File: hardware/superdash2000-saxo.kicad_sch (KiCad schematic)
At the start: 7 parts, among them J1 Molex 34691-0161, U1 L7805

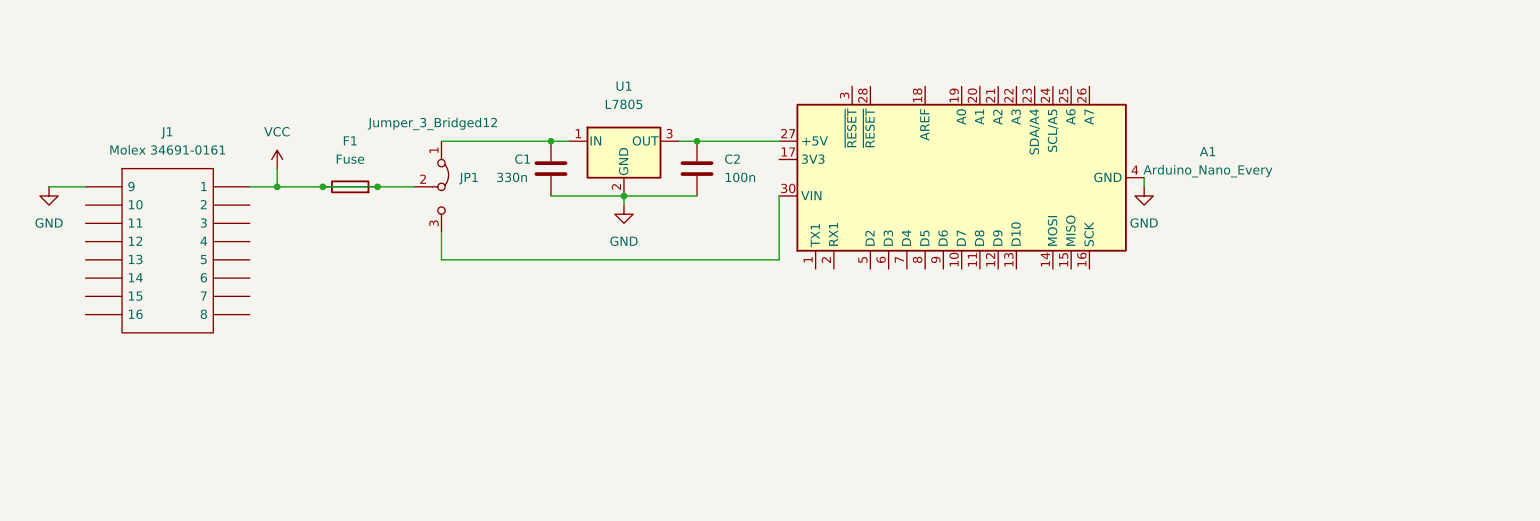
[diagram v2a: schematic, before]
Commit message: hardware: Update schematics
VCC -> +BATT
Add +5V label
Add LCD-SCL label
Add LCD-SDA label

Signed-off-by: Thomas Antonini <antonini.thomas@gmail.com>
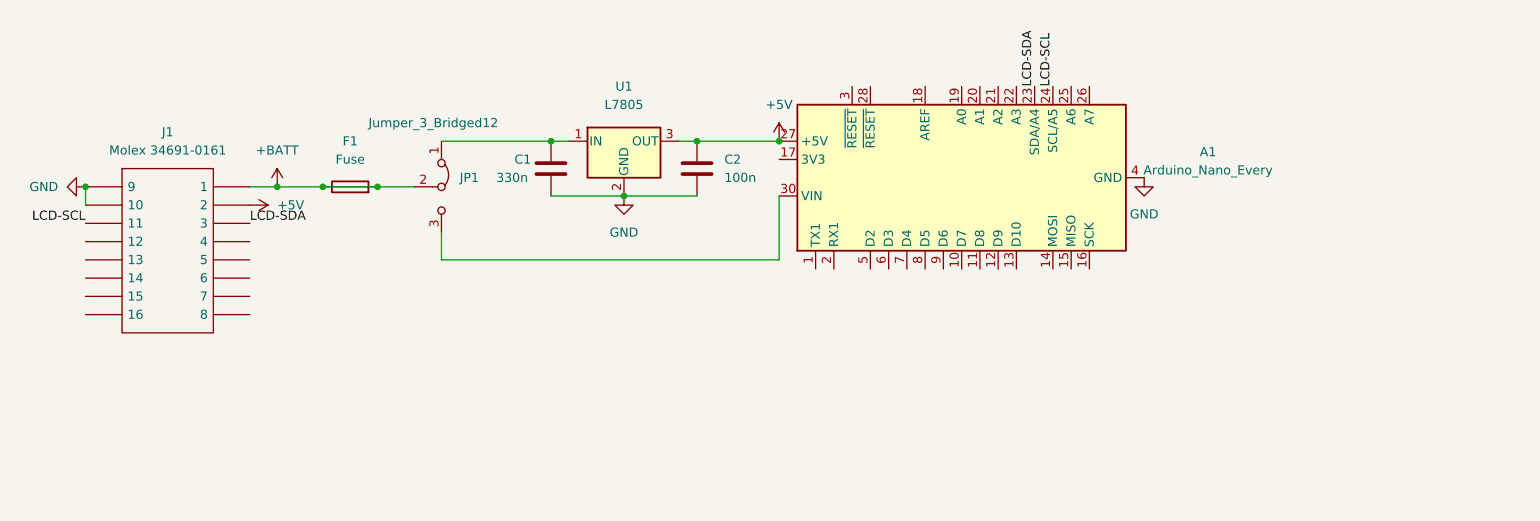
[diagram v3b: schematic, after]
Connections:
- net GND: now also J1.10
- net +5V: now reaches A1.27 (+5V), C2.1, U1.3 (OUT)
- net +5V: now also J1.2
- net LCD-SDA: now reaches A1.23 (SDA/A4)
- net LCD-SDA: now also J1.3
- net LCD-SCL: now reaches A1.24 (SCL/A5)
- net LCD-SCL: now also J1.11
- net VCC renamed +BATT
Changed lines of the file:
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@@
   (junction (at 64.77 64.77) (diameter 0) (color 0 0 0 0)
   )
+  (junction (at 134.62 58.42) (diameter 0) (color 0 0 0 0)
+  )
   (junction (at 123.19 58.42) (diameter 0) (color 0 0 0 0)
   )
   (junction (at 113.03 66.04) (diameter 0) (color 0 0 0 0)
   )
+  (junction (at 38.1 64.77) (diameter 0) (color 0 0 0 0)
+  )
   (junction (at 102.87 58.42) (diameter 0) (color 0 0 0 0)
   )
@@
     (stroke (width 0) (type default) (color 0 0 0 0))
   )
-  (wire (pts (xy 64.77 62.23) (xy 64.77 64.77))
-    (stroke (width 0) (type default) (color 0 0 0 0))
-  )
   (wire (pts (xy 78.74 64.77) (xy 83.82 64.77))
     (stroke (width 0) (type default) (color 0 0 0 0))
@@
     (stroke (width 0) (type default) (color 0 0 0 0))
   )
-  (wire (pts (xy 185.42 63.5) (xy 185.42 64.77))
-    (stroke (width 0) (type default) (color 0 0 0 0))
-  )
   (wire (pts (xy 71.12 64.77) (xy 78.74 64.77))
     (stroke (width 0) (type default) (color 0 0 0 0))
@@
     (stroke (width 0) (type default) (color 0 0 0 0))
   )
-  (wire (pts (xy 33.02 64.77) (xy 38.1 64.77))
-    (stroke (width 0) (type default) (color 0 0 0 0))
-  )
   (wire (pts (xy 102.87 66.04) (xy 113.03 66.04))
     (stroke (width 0) (type default) (color 0 0 0 0))
   )
-  (wire (pts (xy 113.03 66.04) (xy 113.03 67.31))
-    (stroke (width 0) (type default) (color 0 0 0 0))
-  )
   (wire (pts (xy 123.19 58.42) (xy 120.65 58.42))
     (stroke (width 0) (type default) (color 0 0 0 0))
@@
     (stroke (width 0) (type default) (color 0 0 0 0))
   )
+  (wire (pts (xy 38.1 64.77) (xy 38.1 67.31))
+    (stroke (width 0) (type default) (color 0 0 0 0))
+  )
   (wire (pts (xy 64.77 64.77) (xy 71.12 64.77))
     (stroke (width 0) (type default) (color 0 0 0 0))
@@
     (stroke (width 0) (type default) (color 0 0 0 0))
   )
-  (symbol (lib_id "power:GND") (at 185.42 64.77 0) (unit 1)
-    (in_bom yes) (on_board yes) (fields_autoplaced)
-    (property "Reference" "#PWR0101" (id 0) (at 185.42 71.12 0)
-      (effects (font (size 1.27 1.27)) hide)
-    )
-    (property "Value" "GND" (id 1) (at 185.42 69.85 0))
-    (property "Footprint" "" (id 2) (at 185.42 64.77 0)
-      (effects (font (size 1.27 1.27)) hide)
-    )
-    (property "Datasheet" "" (id 3) (at 185.42 64.77 0)
-      (effects (font (size 1.27 1.27)) hide)
-    )
-    (pin "1")
-  )
-  (symbol (lib_id "power:GND") (at 33.02 64.77 0) (unit 1)
-    (in_bom yes) (on_board yes) (fields_autoplaced)
-    (property "Reference" "#PWR?" (id 0) (at 33.02 71.12 0)
-      (effects (font (size 1.27 1.27)) hide)
-    )
-    (property "Value" "GND" (id 1) (at 33.02 69.85 0))
-    (property "Footprint" "" (id 2) (at 33.02 64.77 0)
-      (effects (font (size 1.27 1.27)) hide)
-    )
-    (property "Datasheet" "" (id 3) (at 33.02 64.77 0)
-      (effects (font (size 1.27 1.27)) hide)
-    )
-    (pin "1")
-  )
-  (symbol (lib_id "power:GND") (at 113.03 67.31 0) (unit 1)
-    (in_bom yes) (on_board yes) (fields_autoplaced)
-    (property "Reference" "#PWR0102" (id 0) (at 113.03 73.66 0)
-      (effects (font (size 1.27 1.27)) hide)
-    )
-    (property "Value" "GND" (id 1) (at 113.03 72.39 0))
-    (property "Footprint" "" (id 2) (at 113.03 67.31 0)
-      (effects (font (size 1.27 1.27)) hide)
-    )
-    (property "Datasheet" "" (id 3) (at 113.03 67.31 0)
+  (label "LCD-SDA" (at 170.18 50.8 90)
+    (effects (font (size 1.27 1.27)) (justify left bottom))
+  )
+  (label "LCD-SDA" (at 60.96 69.85 0)
+    (effects (font (size 1.27 1.27)) (justify left bottom))
+  )
+  (label "LCD-SCL" (at 38.1 69.85 180)
+    (effects (font (size 1.27 1.27)) (justify right bottom))
+  )
+  (label "LCD-SCL" (at 172.72 50.8 90)
+    (effects (font (size 1.27 1.27)) (justify left bottom))
+  )
+  (symbol (lib_id "power:GND") (at 185.42 63.5 0) (unit 1)
+    (in_bom yes) (on_board yes) (fields_autoplaced)
+    (property "Reference" "#PWR0101" (id 0) (at 185.42 69.85 0)
+      (effects (font (size 1.27 1.27)) hide)
+    )
+    (property "Value" "GND" (id 1) (at 185.42 68.58 0))
+    (property "Footprint" "" (id 2) (at 185.42 63.5 0)
+      (effects (font (size 1.27 1.27)) hide)
+    )
+    (property "Datasheet" "" (id 3) (at 185.42 63.5 0)
+      (effects (font (size 1.27 1.27)) hide)
+    )
+    (pin "1")
+  )
+  (symbol (lib_id "power:GND") (at 38.1 64.77 270) (unit 1)
+    (in_bom yes) (on_board yes) (fields_autoplaced)
+    (property "Reference" "#PWR0106" (id 0) (at 31.75 64.77 0)
+      (effects (font (size 1.27 1.27)) hide)
+    )
+    (property "Value" "GND" (id 1) (at 34.29 64.7699 90)
+      (effects (font (size 1.27 1.27)) (justify right))
+    )
+    (property "Footprint" "" (id 2) (at 38.1 64.77 0)
+      (effects (font (size 1.27 1.27)) hide)
+    )
+    (property "Datasheet" "" (id 3) (at 38.1 64.77 0)
+      (effects (font (size 1.27 1.27)) hide)
+    )
+    (pin "1")
+  )
+  (symbol (lib_id "power:GND") (at 113.03 66.04 0) (unit 1)
+    (in_bom yes) (on_board yes) (fields_autoplaced)
+    (property "Reference" "#PWR0102" (id 0) (at 113.03 72.39 0)
+      (effects (font (size 1.27 1.27)) hide)
+    )
+    (property "Value" "GND" (id 1) (at 113.03 71.12 0))
+    (property "Footprint" "" (id 2) (at 113.03 66.04 0)
+      (effects (font (size 1.27 1.27)) hide)
+    )
+    (property "Datasheet" "" (id 3) (at 113.03 66.04 0)
       (effects (font (size 1.27 1.27)) hide)
     )
@@
     (pin "9")
   )
+  (symbol (lib_id "power:+BATT") (at 64.77 64.77 0) (unit 1)
+    (in_bom yes) (on_board yes) (fields_autoplaced)
+    (property "Reference" "#PWR0103" (id 0) (at 64.77 68.58 0)
+      (effects (font (size 1.27 1.27)) hide)
+    )
+    (property "Value" "+BATT" (id 1) (at 64.77 59.69 0))
+    (property "Footprint" "" (id 2) (at 64.77 64.77 0)
+      (effects (font (size 1.27 1.27)) hide)
+    )
+    (property "Datasheet" "" (id 3) (at 64.77 64.77 0)
+      (effects (font (size 1.27 1.27)) hide)
+    )
+    (pin "1")
+  )
+  (symbol (lib_id "power:+5V") (at 134.62 58.42 0) (unit 1)
+    (in_bom yes) (on_board yes) (fields_autoplaced)
+    (property "Reference" "#PWR0105" (id 0) (at 134.62 62.23 0)
+      (effects (font (size 1.27 1.27)) hide)
+    )
+    (property "Value" "+5V" (id 1) (at 134.62 53.34 0))
+    (property "Footprint" "" (id 2) (at 134.62 58.42 0)
+      (effects (font (size 1.27 1.27)) hide)
+    )
+    (property "Datasheet" "" (id 3) (at 134.62 58.42 0)
+      (effects (font (size 1.27 1.27)) hide)
+    )
+    (pin "1")
+  )
+  (symbol (lib_id "power:+5V") (at 60.96 67.31 270) (unit 1)
+    (in_bom yes) (on_board yes) (fields_autoplaced)
+    (property "Reference" "#PWR0104" (id 0) (at 57.15 67.31 0)
+      (effects (font (size 1.27 1.27)) hide)
+    )
+    (property "Value" "+5V" (id 1) (at 64.77 67.3099 90)
+      (effects (font (size 1.27 1.27)) (justify left))
+    )
+    (property "Footprint" "" (id 2) (at 60.96 67.31 0)
+      (effects (font (size 1.27 1.27)) hide)
+    )
+    (property "Datasheet" "" (id 3) (at 60.96 67.31 0)
+      (effects (font (size 1.27 1.27)) hide)
+    )
+    (pin "1")
+  )
   (symbol (lib_id "Device:C") (at 102.87 62.23 0) (unit 1)
     (in_bom yes) (on_board yes)
@@
     (pin "2")
   )
-  (symbol (lib_id "power:VCC") (at 64.77 62.23 0) (unit 1)
-    (in_bom yes) (on_board yes)
-    (property "Reference" "#PWR0103" (id 0) (at 64.77 66.04 0)
-      (effects (font (size 1.27 1.27)) hide)
-    )
-    (property "Value" "VCC" (id 1) (at 64.77 57.15 0))
-    (property "Footprint" "" (id 2) (at 64.77 62.23 0)
-      (effects (font (size 1.27 1.27)) hide)
-    )
-    (property "Datasheet" "" (id 3) (at 64.77 62.23 0)
-      (effects (font (size 1.27 1.27)) hide)
-    )
-    (pin "1")
-  )
   (sheet_instances
     (path "/" (page "1"))
@@
       (reference "#PWR0102") (unit 1) (value "GND") (footprint "")
     )
-    (path "/f16717c9-4da6-4641-a01d-d15d2a023c10"
-      (reference "#PWR0103") (unit 1) (value "VCC") (footprint "")
+    (path "/9b390981-9820-4a6d-9d6b-273f0a2642eb"
+      (reference "#PWR0103") (unit 1) (value "+BATT") (footprint "")
+    )
+    (path "/d452a94e-41da-4920-9425-e3d186a49a40"
+      (reference "#PWR0104") (unit 1) (value "+5V") (footprint "")
+    )
+    (path "/c6790040-edb4-45c5-8280-6a3e09717dec"
+      (reference "#PWR0105") (unit 1) (value "+5V") (footprint "")
     )
     (path "/28bd7130-fb8b-4bdb-a9c1-61b7bb039857"
-      (reference "#PWR?") (unit 1) (value "GND") (footprint "")
+      (reference "#PWR0106") (unit 1) (value "GND") (footprint "")
     )
     (path "/65c02b6a-4170-4a63-9193-eec01920d5e8"

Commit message: hardware: Add lcd potentiometer
Signed-off-by: Thomas Antonini <antonini.thomas@gmail.com>
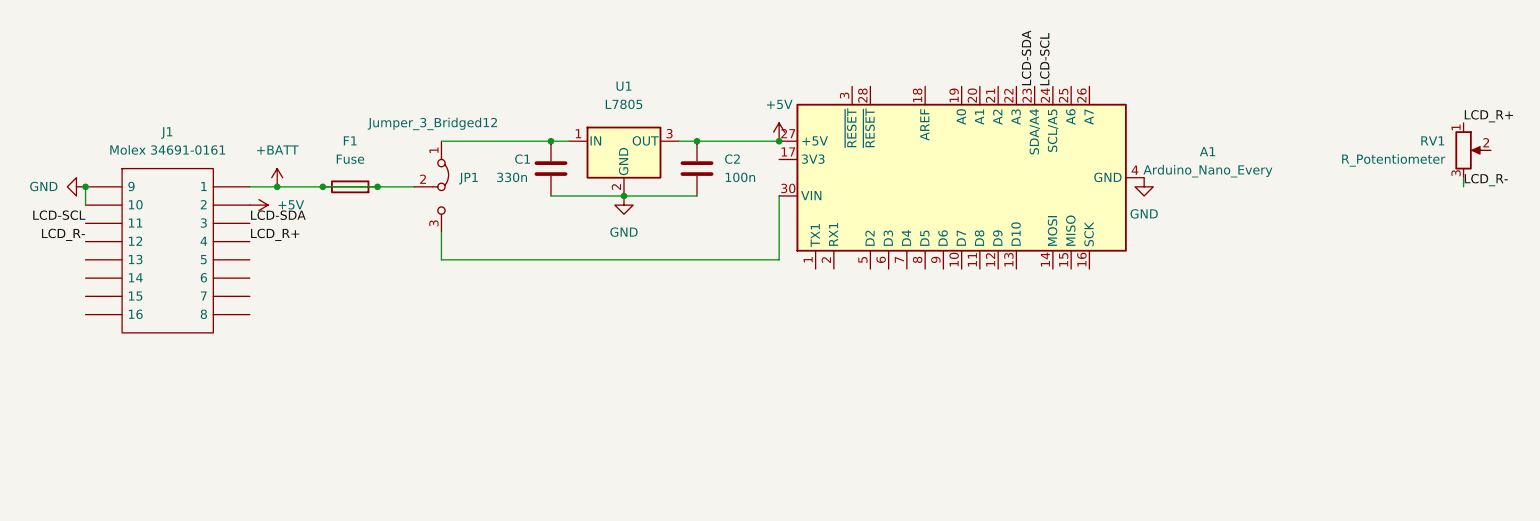
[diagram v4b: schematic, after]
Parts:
- added RV1: R_Potentiometer, symbol Device:R_Potentiometer
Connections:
- net LCD_R-: now reaches J1.12
- net LCD_R-: now also RV1.3
- net LCD_R+: now reaches J1.4
- net LCD_R+: now also RV1.1
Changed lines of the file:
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@@
+    (stroke (width 0) (type default) (color 0 0 0 0))
+  )
+  (wire (pts (xy 229.87 64.77) (xy 229.87 63.5))
     (stroke (width 0) (type default) (color 0 0 0 0))
   )
@@
   )
   (label "LCD-SDA" (at 170.18 50.8 90)
+    (effects (font (size 1.27 1.27)) (justify left bottom))
+  )
+  (label "LCD_R+" (at 60.96 72.39 0)
+    (effects (font (size 1.27 1.27)) (justify left bottom))
+  )
+  (label "LCD_R+" (at 229.87 55.88 0)
     (effects (font (size 1.27 1.27)) (justify left bottom))
   )
@@
     (effects (font (size 1.27 1.27)) (justify right bottom))
   )
+  (label "LCD_R-" (at 38.1 72.39 180)
+    (effects (font (size 1.27 1.27)) (justify right bottom))
+  )
   (label "LCD-SCL" (at 172.72 50.8 90)
+    (effects (font (size 1.27 1.27)) (justify left bottom))
+  )
+  (label "LCD_R-" (at 229.87 64.77 0)
     (effects (font (size 1.27 1.27)) (justify left bottom))
   )
@@
     (pin "9")
   )
+  (symbol (lib_id "Device:R_Potentiometer") (at 229.87 59.69 0) (unit 1)
+    (in_bom yes) (on_board yes) (fields_autoplaced)
+    (property "Reference" "RV1" (id 0) (at 227.33 58.4199 0)
+      (effects (font (size 1.27 1.27)) (justify right))
+    )
+    (property "Value" "R_Potentiometer" (id 1) (at 227.33 60.9599 0)
+      (effects (font (size 1.27 1.27)) (justify right))
+    )
+    (property "Footprint" "" (id 2) (at 229.87 59.69 0)
+      (effects (font (size 1.27 1.27)) hide)
+    )
+    (property "Datasheet" "~" (id 3) (at 229.87 59.69 0)
+      (effects (font (size 1.27 1.27)) hide)
+    )
+    (pin "1")
+    (pin "2")
+    (pin "3")
+  )
   (symbol (lib_id "power:+BATT") (at 64.77 64.77 0) (unit 1)
     (in_bom yes) (on_board yes) (fields_autoplaced)
@@
       (reference "JP1") (unit 1) (value "Jumper_3_Bridged12") (footprint "")
     )
+    (path "/8f188f22-a5b9-4f36-a20f-c9a07bb49266"
+      (reference "RV1") (unit 1) (value "R_Potentiometer") (footprint "")
+    )
     (path "/4dcd0dda-1663-4b04-85dd-f6fe52c14280"

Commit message: hardware: Rename LCD-Sxx to LCD_Sxx
Signed-off-by: Thomas Antonini <antonini.thomas@gmail.com>
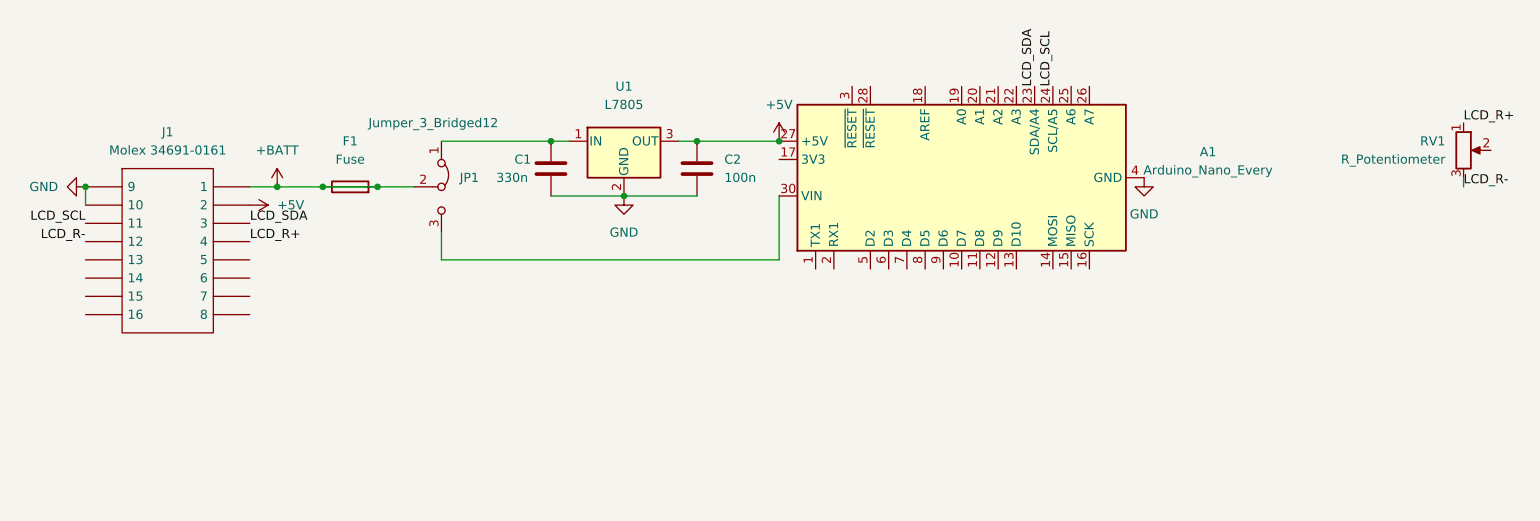
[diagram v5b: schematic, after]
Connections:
- net LCD-SCL renamed LCD_SCL
- net LCD-SDA renamed LCD_SDA
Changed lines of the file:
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@@
     (stroke (width 0) (type default) (color 0 0 0 0))
   )
-  (label "LCD-SDA" (at 170.18 50.8 90)
+  (label "LCD_SDA" (at 170.18 50.8 90)
     (effects (font (size 1.27 1.27)) (justify left bottom))
   )
@@
     (effects (font (size 1.27 1.27)) (justify left bottom))
   )
-  (label "LCD-SDA" (at 60.96 69.85 0)
+  (label "LCD_SDA" (at 60.96 69.85 0)
     (effects (font (size 1.27 1.27)) (justify left bottom))
   )
-  (label "LCD-SCL" (at 38.1 69.85 180)
+  (label "LCD_SCL" (at 38.1 69.85 180)
     (effects (font (size 1.27 1.27)) (justify right bottom))
   )
@@
     (effects (font (size 1.27 1.27)) (justify right bottom))
   )
-  (label "LCD-SCL" (at 172.72 50.8 90)
+  (label "LCD_SCL" (at 172.72 50.8 90)
     (effects (font (size 1.27 1.27)) (justify left bottom))
   )
